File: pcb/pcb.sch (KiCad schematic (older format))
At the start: 4 parts, among them P1 CONN_02X03, P10 TST, P8 TST, P9 TST

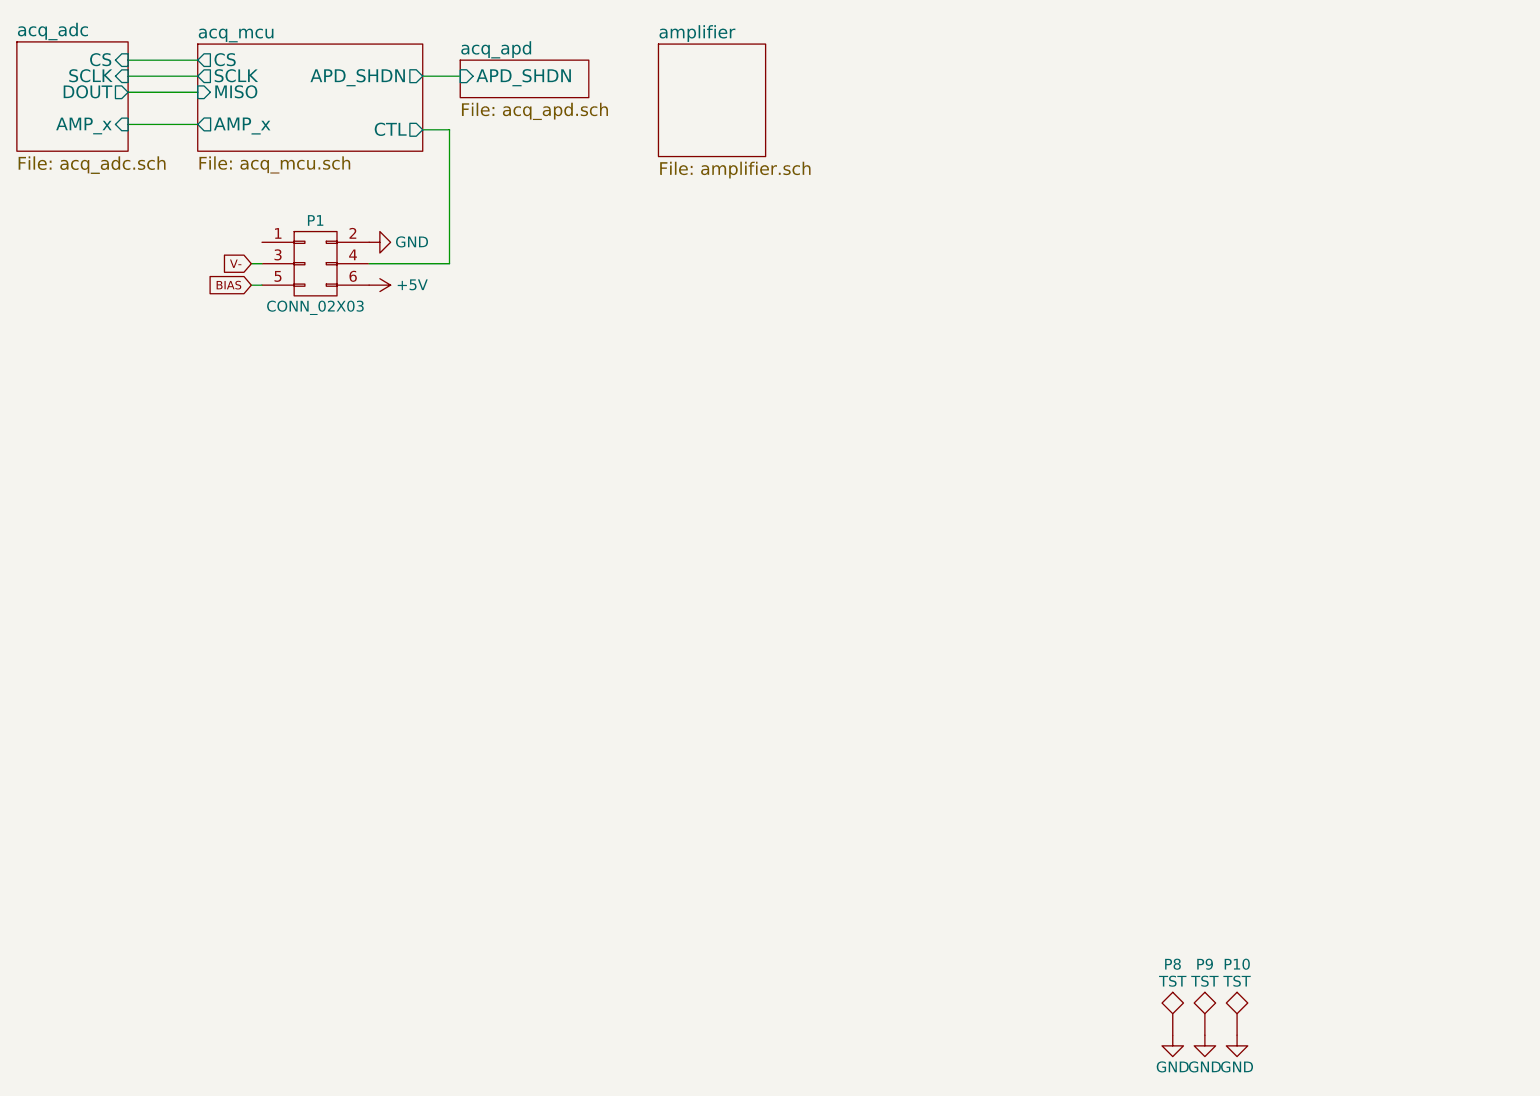
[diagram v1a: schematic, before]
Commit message: pcb: Update to the current iteration
Looks like I forgot to commit the changes made for manufacturing...
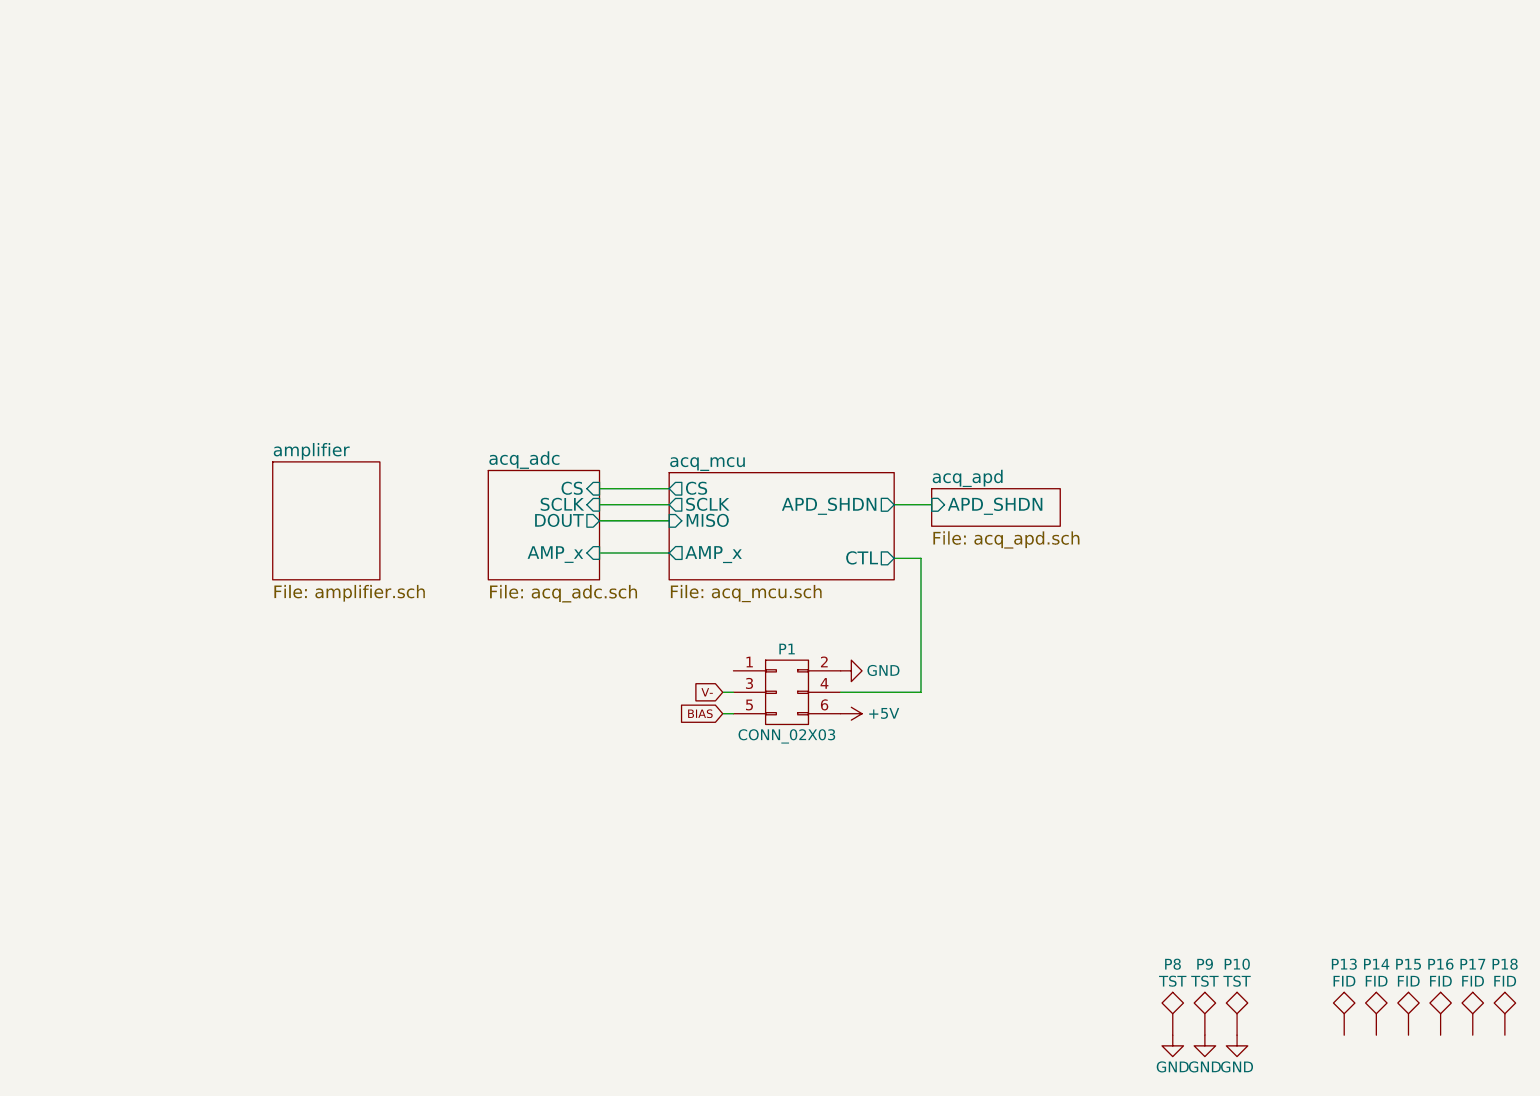
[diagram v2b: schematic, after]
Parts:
- added P13, P14, P15, P16, P17, P18: FID, Fiducials:Fiducial_1mm_Dia_2.54mm_Outer_CopperTop, symbol TST
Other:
- moved on the sheet: P1
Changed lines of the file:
@@
 EESchema Schematic File Version 2
+LIBS:pcb-rescue
 LIBS:power
 LIBS:device
@@
 $EndComp
 $Sheet
-S 2856 1540 519  510
+S 5056 3540 519  510
 U 5728F439
 F0 "acq_adc" 60
 F1 "acq_adc.sch" 60
-F2 "CS" I R 3375 1625 59
-F3 "SCLK" I R 3375 1700 59
-F4 "DOUT" O R 3375 1775 59
-F5 "AMP_x" I R 3375 1925 59
-$EndSheet
-$Sheet
-S 3700 1550 1050 500
+F2 "CS" I R 5575 3625 59
+F3 "SCLK" I R 5575 3700 59
+F4 "DOUT" O R 5575 3775 59
+F5 "AMP_x" I R 5575 3925 59
+$EndSheet
+$Sheet
+S 5900 3550 1050 500
 U 572D32D1
 F0 "acq_mcu" 59
 F1 "acq_mcu.sch" 59
-F2 "SCLK" O L 3700 1700 59
-F3 "CS" O L 3700 1625 59
-F4 "MISO" I L 3700 1775 59
-F5 "APD_SHDN" O R 4750 1700 60
-F6 "AMP_x" O L 3700 1925 60
-F7 "CTL" O R 4750 1950 60
-$EndSheet
-$Sheet
-S 4925 1625 600  175
+F2 "SCLK" O L 5900 3700 59
+F3 "CS" O L 5900 3625 59
+F4 "MISO" I L 5900 3775 59
+F5 "APD_SHDN" O R 6950 3700 60
+F6 "AMP_x" O L 5900 3925 60
+F7 "CTL" O R 6950 3950 60
+$EndSheet
+$Sheet
+S 7125 3625 600  175
 U 572E43F7
 F0 "acq_apd" 59
 F1 "acq_apd.sch" 59
-F2 "APD_SHDN" I L 4925 1700 60
-$EndSheet
-$Sheet
-S 5850 1550 500  525
+F2 "APD_SHDN" I L 7125 3700 60
+$EndSheet
+$Sheet
+S 4050 3500 500  550
 U 572EA088
 F0 "amplifier" 59
@@
 $EndSheet
 Wire Wire Line
-	3375 1925 3700 1925
-Wire Wire Line
-	3700 1775 3375 1775
-Wire Wire Line
-	3375 1700 3700 1700
-Wire Wire Line
-	3700 1625 3375 1625
-Wire Wire Line
-	4925 1700 4750 1700
+	5575 3925 5900 3925
+Wire Wire Line
+	5900 3775 5575 3775
+Wire Wire Line
+	5575 3700 5900 3700
+Wire Wire Line
+	5900 3625 5575 3625
+Wire Wire Line
+	7125 3700 6950 3700
 $Comp
 L GND #PWR1
 U 1 1 57373BE5
-P 4500 2475
-F 0 "#PWR1" H 4500 2225 50  0001 C CNN
-F 1 "GND" V 4500 2275 50  0000 C CNN
-F 2 "" H 4500 2475 50  0000 C CNN
-F 3 "" H 4500 2475 50  0000 C CNN
-	1    4500 2475
+P 6700 4475
+F 0 "#PWR1" H 6700 4225 50  0001 C CNN
+F 1 "GND" V 6700 4275 50  0000 C CNN
+F 2 "" H 6700 4475 50  0000 C CNN
+F 3 "" H 6700 4475 50  0000 C CNN
+	1    6700 4475
 	0    -1   -1   0
 $EndComp
@@
 L +5V #PWR2
 U 1 1 57373BEB
-P 4500 2675
-F 0 "#PWR2" H 4500 2525 50  0001 C CNN
-F 1 "+5V" V 4500 2875 50  0000 C CNN
-F 2 "" H 4500 2675 50  0000 C CNN
-F 3 "" H 4500 2675 50  0000 C CNN
-	1    4500 2675
+P 6700 4675
+F 0 "#PWR2" H 6700 4525 50  0001 C CNN
+F 1 "+5V" V 6700 4875 50  0000 C CNN
+F 2 "" H 6700 4675 50  0000 C CNN
+F 3 "" H 6700 4675 50  0000 C CNN
+	1    6700 4675
 	0    1    1    0
 $EndComp
-Text GLabel 3950 2675 0    39   Input ~ 0
+Text GLabel 6150 4675 0    39   Input ~ 0
 BIAS
 $Comp
 L CONN_02X03 P1
 U 1 1 57373BF2
-P 4250 2575
-F 0 "P1" H 4250 2775 50  0000 C CNN
-F 1 "CONN_02X03" H 4250 2375 50  0000 C CNN
-F 2 "footprints:CONN_02x03_EDGE" H 4250 1375 50  0001 C CNN
-F 3 "" H 4250 1375 50  0000 C CNN
-	1    4250 2575
-	1    0    0    -1
-$EndComp
-Text GLabel 3950 2575 0    39   Input ~ 0
+P 6450 4575
+F 0 "P1" H 6450 4775 50  0000 C CNN
+F 1 "CONN_02X03" H 6450 4375 50  0000 C CNN
+F 2 "footprints:CONN_02x03_EDGE" H 6450 3375 50  0001 C CNN
+F 3 "" H 6450 3375 50  0000 C CNN
+	1    6450 4575
+	1    0    0    -1
+$EndComp
+Text GLabel 6150 4575 0    39   Input ~ 0
 V-
 Wire Wire Line
-	3950 2575 4000 2575
-Wire Wire Line
-	3950 2675 4000 2675
-Wire Wire Line
-	4750 1950 4875 1950
-Wire Wire Line
-	4875 1950 4875 2575
-Wire Wire Line
-	4875 2575 4500 2575
+	6150 4575 6200 4575
+Wire Wire Line
+	6150 4675 6200 4675
+Wire Wire Line
+	6950 3950 7075 3950
+Wire Wire Line
+	7075 3950 7075 4575
+Wire Wire Line
+	7075 4575 6700 4575
+$Comp
+L TST P13
+U 1 1 58BE0697
+P 9050 6175
+F 0 "P13" H 9050 6475 50  0000 C BNN
+F 1 "FID" H 9050 6425 50  0000 C CNN
+F 2 "Fiducials:Fiducial_1mm_Dia_2.54mm_Outer_CopperTop" H 9050 6175 50  0001 C CNN
+F 3 "" H 9050 6175 50  0000 C CNN
+	1    9050 6175
+	1    0    0    -1
+$EndComp
+$Comp
+L TST P14
+U 1 1 58BE080E
+P 9200 6175
+F 0 "P14" H 9200 6475 50  0000 C BNN
+F 1 "FID" H 9200 6425 50  0000 C CNN
+F 2 "Fiducials:Fiducial_1mm_Dia_2.54mm_Outer_CopperTop" H 9200 6175 50  0001 C CNN
+F 3 "" H 9200 6175 50  0000 C CNN
+	1    9200 6175
+	1    0    0    -1
+$EndComp
+$Comp
+L TST P15
+U 1 1 58BE0938
+P 9350 6175
+F 0 "P15" H 9350 6475 50  0000 C BNN
+F 1 "FID" H 9350 6425 50  0000 C CNN
+F 2 "Fiducials:Fiducial_1mm_Dia_2.54mm_Outer_CopperTop" H 9350 6175 50  0001 C CNN
+F 3 "" H 9350 6175 50  0000 C CNN
+	1    9350 6175
+	1    0    0    -1
+$EndComp
+$Comp
+L TST P16
+U 1 1 58C457FC
+P 9500 6175
+F 0 "P16" H 9500 6475 50  0000 C BNN
+F 1 "FID" H 9500 6425 50  0000 C CNN
+F 2 "Fiducials:Fiducial_1mm_Dia_2.54mm_Outer_CopperTop" H 9500 6175 50  0001 C CNN
+F 3 "" H 9500 6175 50  0000 C CNN
+	1    9500 6175
+	1    0    0    -1
+$EndComp
+$Comp
+L TST P17
+U 1 1 58C45802
+P 9650 6175
+F 0 "P17" H 9650 6475 50  0000 C BNN
+F 1 "FID" H 9650 6425 50  0000 C CNN
+F 2 "Fiducials:Fiducial_1mm_Dia_2.54mm_Outer_CopperTop" H 9650 6175 50  0001 C CNN
+F 3 "" H 9650 6175 50  0000 C CNN
+	1    9650 6175
+	1    0    0    -1
+$EndComp
+$Comp
+L TST P18
+U 1 1 58C45808
+P 9800 6175
+F 0 "P18" H 9800 6475 50  0000 C BNN
+F 1 "FID" H 9800 6425 50  0000 C CNN
+F 2 "Fiducials:Fiducial_1mm_Dia_2.54mm_Outer_CopperTop" H 9800 6175 50  0001 C CNN
+F 3 "" H 9800 6175 50  0000 C CNN
+	1    9800 6175
+	1    0    0    -1
+$EndComp
 $EndSCHEMATC
